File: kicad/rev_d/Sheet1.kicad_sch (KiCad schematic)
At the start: 159 parts, among them J1 JUMPER, J2 JUMPER, J3 JUMPER, J4 JUMPER, J7 JUMPER, Q1 QUARTZ, X1 FDD34M, X2 IDE40M, X3 IDC26LPT, X7 DB15VGA, X8 PLB1-4I, X9 PLB1-2

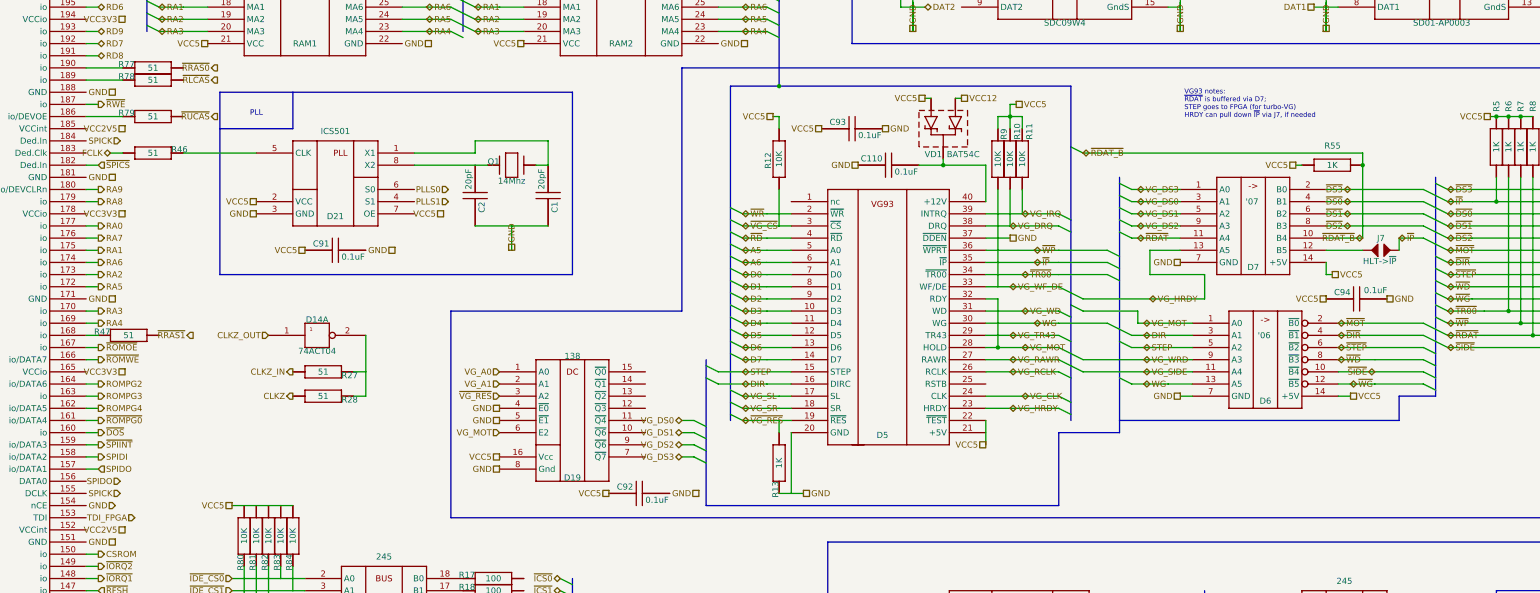
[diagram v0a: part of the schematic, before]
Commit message: pentevo: small update to converted kicad sch
git-svn-id: svn://localhost/local-pentevo@1165 c6c76956-fad2-4150-a3a9-ea0a427205ba
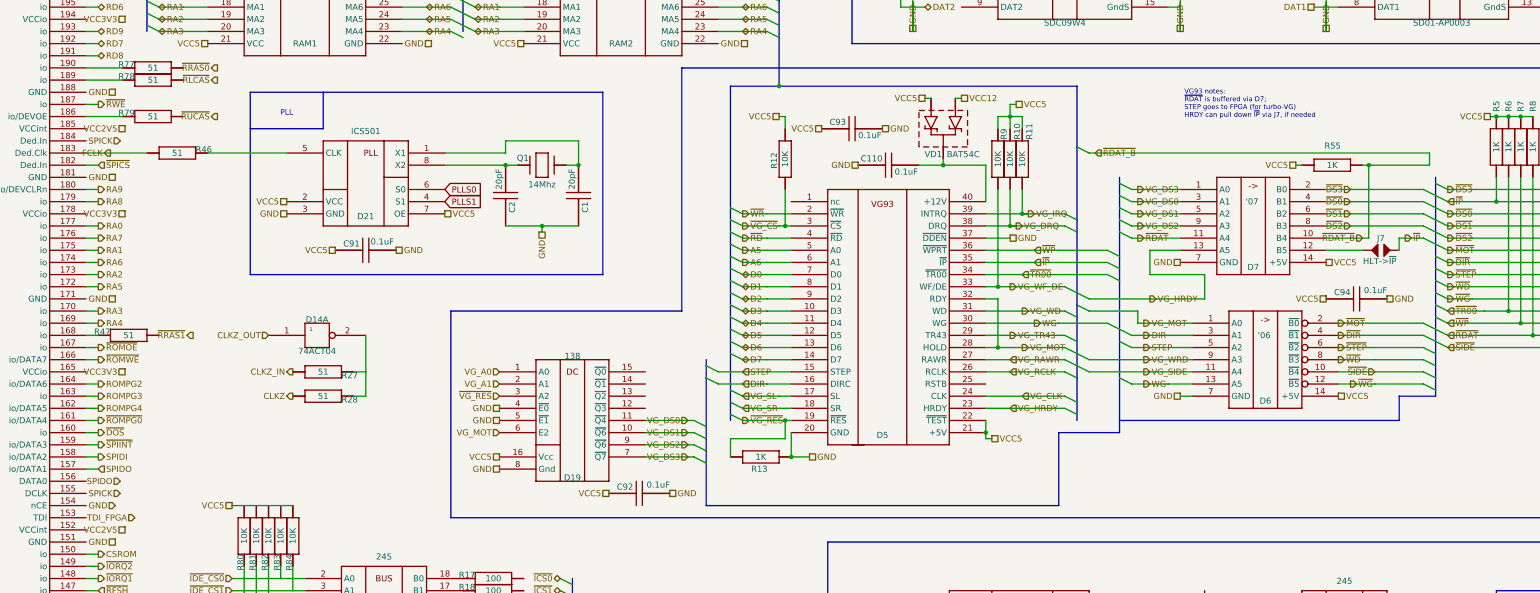
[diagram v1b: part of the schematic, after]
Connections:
- net FCLK: now also D2.183 (Ded.Clk)
- net GND: now also C91.2, C92.2, D5.20 (GND)
- net PLLS0: now also D21.6 (S0)
- net PLLS1: now also D21.4 (S1)
- net VCC5: now also D21.7 (OE), D5.21 (+5V)
- net VG_DS0: now also D19.11 (~{Q4})
- net VG_DS1: now also D19.10 (~{Q6})
- net VG_DS2: now also D19.9 (~{Q6})
- net VG_DS3: now also D19.7 (~{Q7})
- net at D21.8 (X2), Q1.A: now also C2.2
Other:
- moved on the sheet: C1, C2, C91, D21, Q1, R12, R13, R46

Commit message: pentevo: small update to converted kicad sch (IDE)
git-svn-id: svn://localhost/local-pentevo@1166 c6c76956-fad2-4150-a3a9-ea0a427205ba
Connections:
- net GND: now also C90.2, D10.19 (~{OE}), D11.19 (~{OE})
- net ID0: now also X2.17 (D00)
- net ID1: now also X2.15 (D01)
- net ID10: now also X2.8 (D10)
- net ID11: now also X2.10 (D11)
- net ID12: now also D10.2 (A0), X2.12 (D12)
- net ID13: now also D10.4 (A2), X2.14 (D13)
- net ID14: now also D10.6 (A4), X2.16 (D14)
- net ID15: now also D10.8 (A6), X2.18 (D15)
- net ID2: now also X2.13 (D02)
- net ID3: now also X2.11 (D03)
- net ID4: now also X2.9 (D04)
- net ID5: now also X2.7 (D05)
- net ID6: now also X2.5 (D06)
- net ID7: now also X2.3 (D07)
- net ID8: now also X2.4 (D08)
- net ID9: now also X2.6 (D09)
- net IDE_DIR: now also D10.1 (T/~{R}), R85.2 (i/o1)
- net IDE_RDY: now also R20.1 (i/o)
- net VCC5: now also R19.1 (i/o), R80.1 (i/o), R81.1 (i/o), R82.1 (i/o), R85.1 (i/o)
- net ~{ICS0}: now also R17.1 (i/o), X2.37 (~{CS0})
- net ~{ICS1}: now also R18.1 (i/o), X2.38 (~{CS1})
- net ~{IRES}: now also X2.1 (~{RESET})
- net ~{IWR}: now also R15.1 (i/o), X2.23 (~{DIOW})
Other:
- moved on the sheet: C90, D10, D11, D12, D14A, J1, R15, R16, R17, R18, R19, R20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

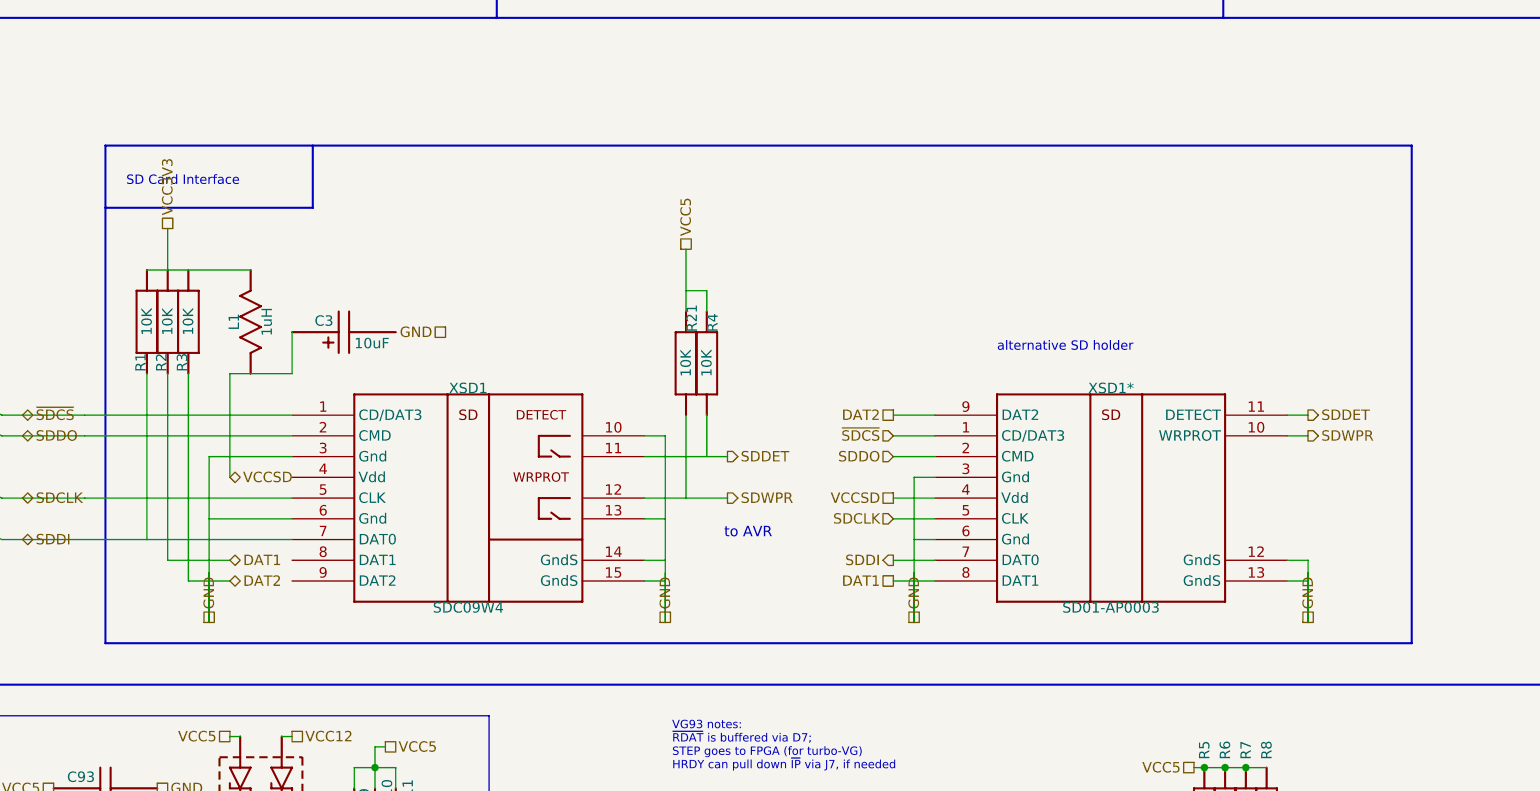
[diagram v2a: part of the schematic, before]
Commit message: pentevo: small update to converted kicad sch (SD)
git-svn-id: svn://localhost/local-pentevo@1167 c6c76956-fad2-4150-a3a9-ea0a427205ba
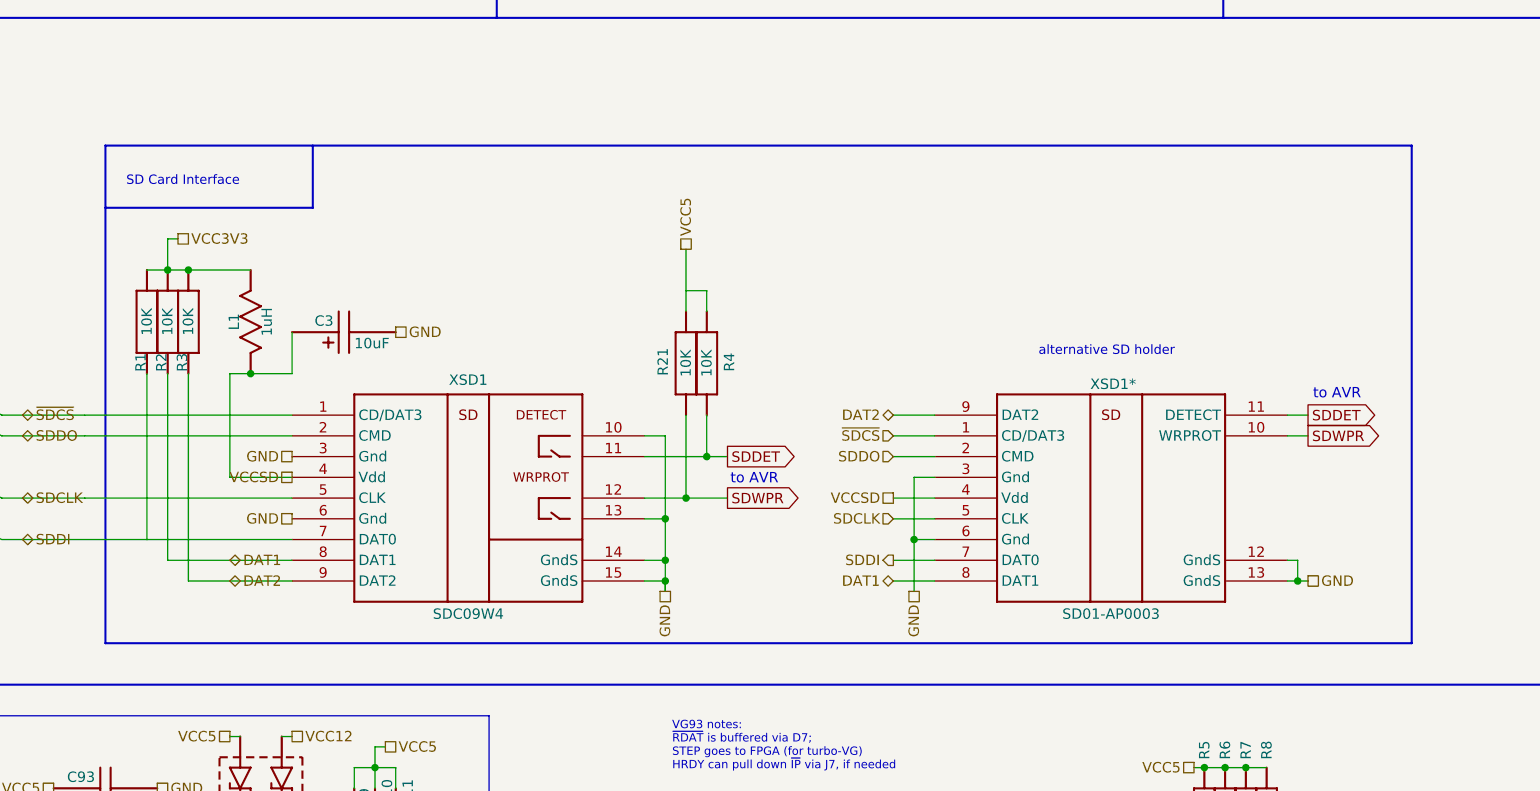
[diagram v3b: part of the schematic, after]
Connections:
- net DAT1: now also XSD1.8 (DAT1)
- net DAT2: now also XSD1.9 (DAT2)
- net GND: now also C3.2
- net SDDET: now also R4.1 (i/o)
- net SDWPR: now also R21.1 (i/o)
- net VCC3V3: now also L1.1, R1.1 (i/o), R3.1 (i/o)
- net VCCSD: now also L1.2, XSD1.4 (Vdd)

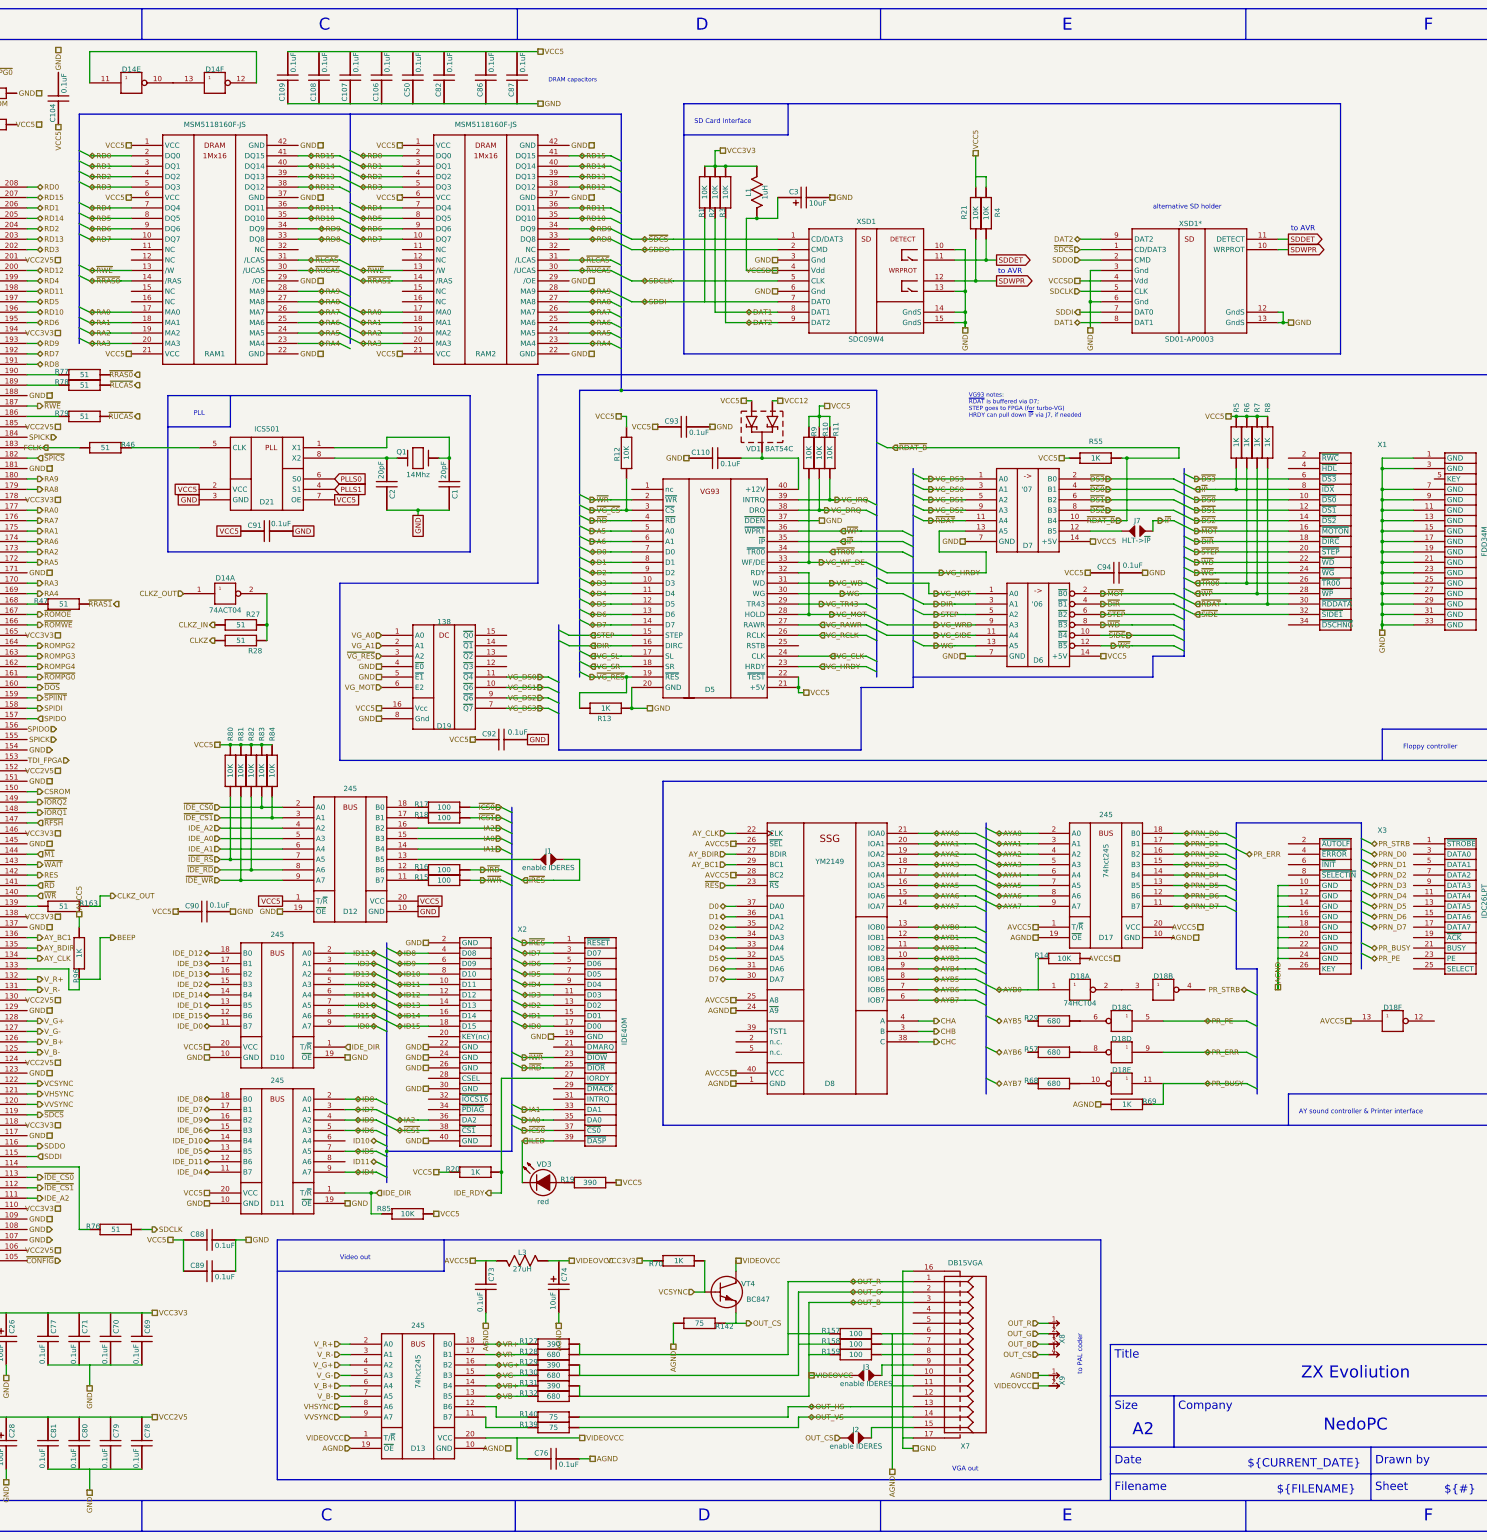
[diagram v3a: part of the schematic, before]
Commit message: pentevo: small update to converted kicad sch (AY, video)
git-svn-id: svn://localhost/local-pentevo@1168 c6c76956-fad2-4150-a3a9-ea0a427205ba
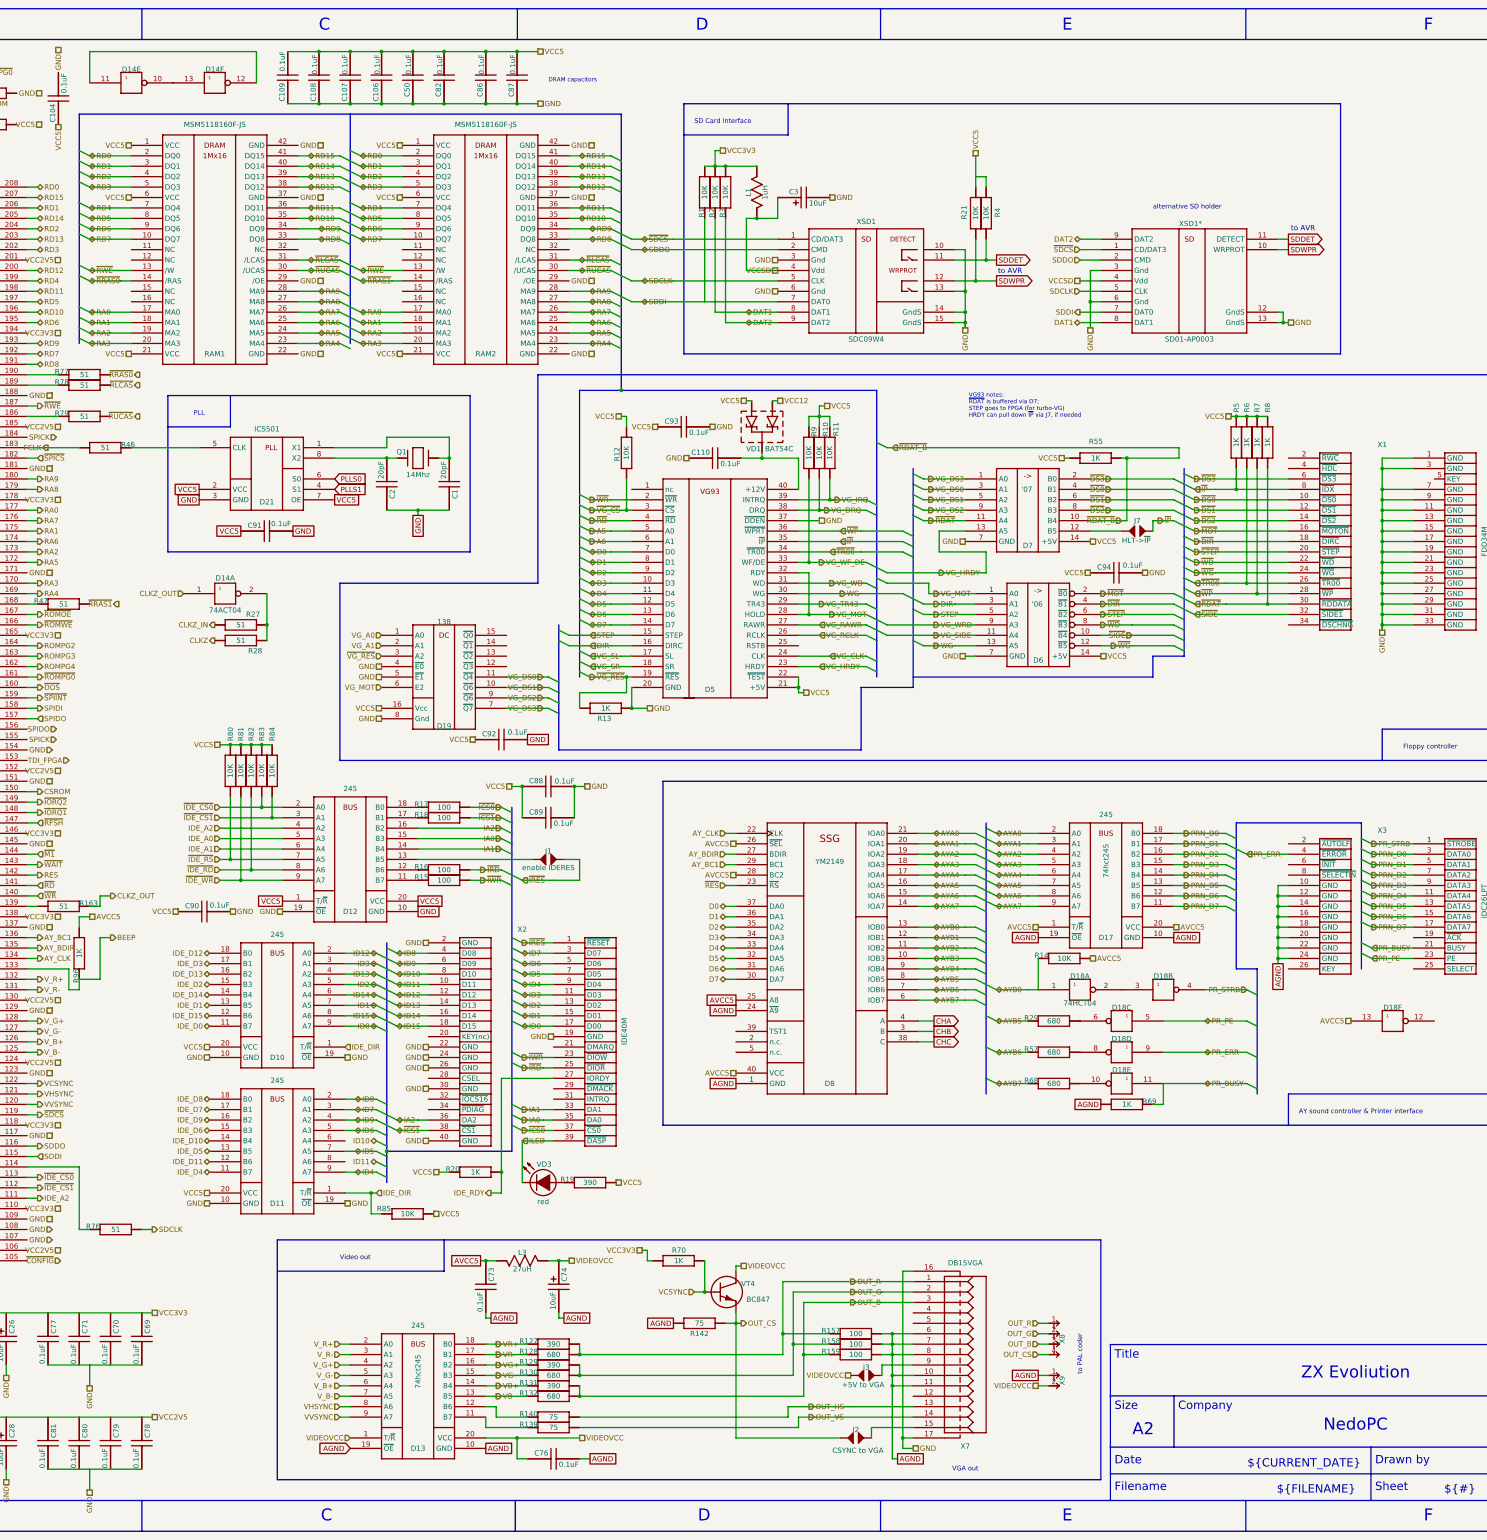
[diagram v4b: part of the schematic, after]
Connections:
- net AGND: now also D13.10 (GND), D17.10 (GND), R157.1 (i/o), X7.6
- net AVCC5: now also C73.1, D17.20 (VCC), R14.1 (i/o)
- net AYB5: now also R29.2 (i/o1)
- net AYB6: now also R57.2 (i/o1)
- net AYB7: now also R68.2 (i/o1)
- net GND: now also C106.1, C107.1, C108.1, C82.1, C86.1, X3.23 (PE)
- net OUT_B: no longer C76.1, D13.1 (T/~{R}), D13.20 (VCC), J3.0 (1), L3.1, VT4.3 (collector), X9.2
- net OUT_CS: now also VT4.2 (emitter)
- net OUT_G: now also R158.2 (i/o1)
- net OUT_R: now also R157.2 (i/o1)
- net PRN_D0: now also X3.3 (DATA0)
- net PRN_D1: now also X3.5 (DATA1)
- net PRN_D2: now also X3.7 (DATA2)
- net PRN_D3: now also X3.9 (DATA3)
- net PRN_D4: now also X3.11 (DATA4)
- net PRN_D5: now also X3.13 (DATA5)
- net PRN_D6: now also X3.15 (DATA6)
- net PRN_D7: now also X3.17 (DATA7)
- net PR_BUSY: now also X3.21 (BUSY)
- net PR_ERR: now also X3.4 (~{ERROR})
- net PR_STRB: now also D18.4, X3.1 (~{STROBE})
- net VCC5: now also C106.2, C107.2, C108.2, C82.2, C86.2
- net VIDEOVCC: now reaches C74.1
- net VIDEOVCC: now also C76.1, D13.1 (T/~{R}), D13.20 (VCC), J3.0 (1), L3.1, VT4.3 (collector), X9.2
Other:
- moved on the sheet: C88, C89

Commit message: pentevo: small update to converted kicad sch (DRAM)
git-svn-id: svn://localhost/local-pentevo@1169 c6c76956-fad2-4150-a3a9-ea0a427205ba
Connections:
- net GND: now also RAM1.22 (GND), RAM1.29 (/OE), RAM1.37 (GND), RAM1.42 (GND), RAM2.22 (GND), RAM2.29 (/OE), RAM2.37 (GND), RAM2.42 (GND)
